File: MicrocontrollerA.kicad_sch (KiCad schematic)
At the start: 40 parts, among them J1 SWD Connector, J13 USB_B_Micro, SW1 SW_Push, SW2 SW_SPDT, SW3 SW_SPDT, U1 STM32F446RCTx, U5 TVS0500DRV, U6 TLV1117-33, Y1 25 MHz

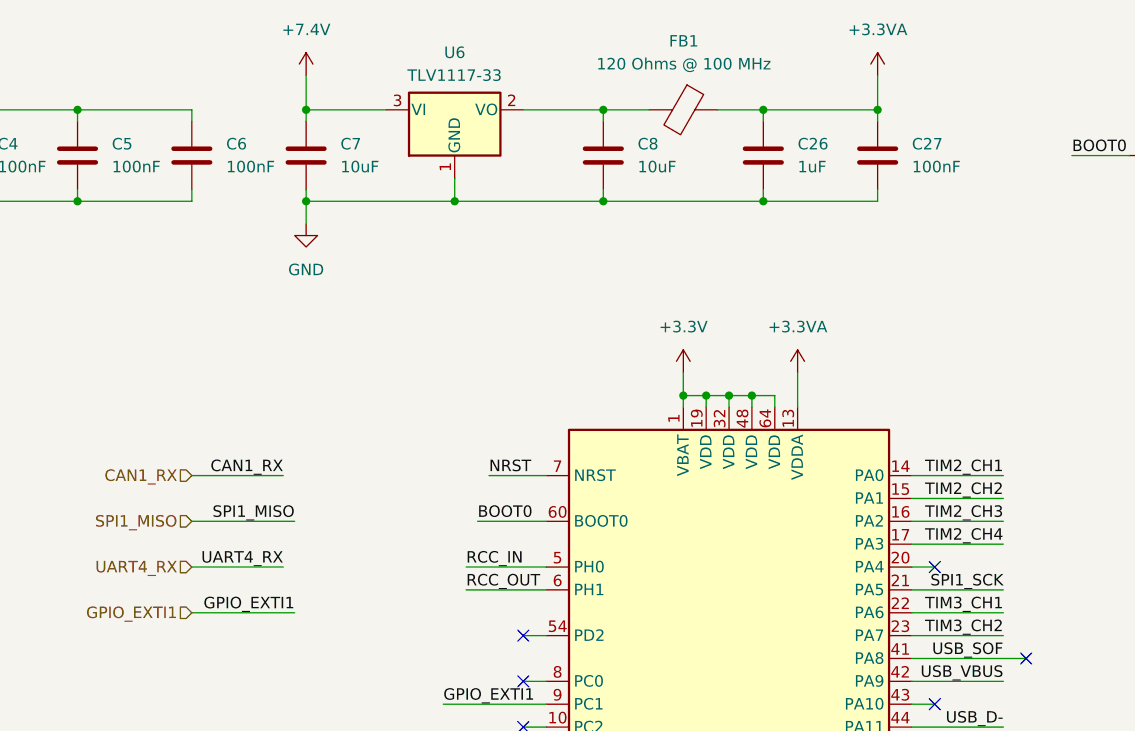
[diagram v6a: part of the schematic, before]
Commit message: Remove LDO and connect FB to switching output
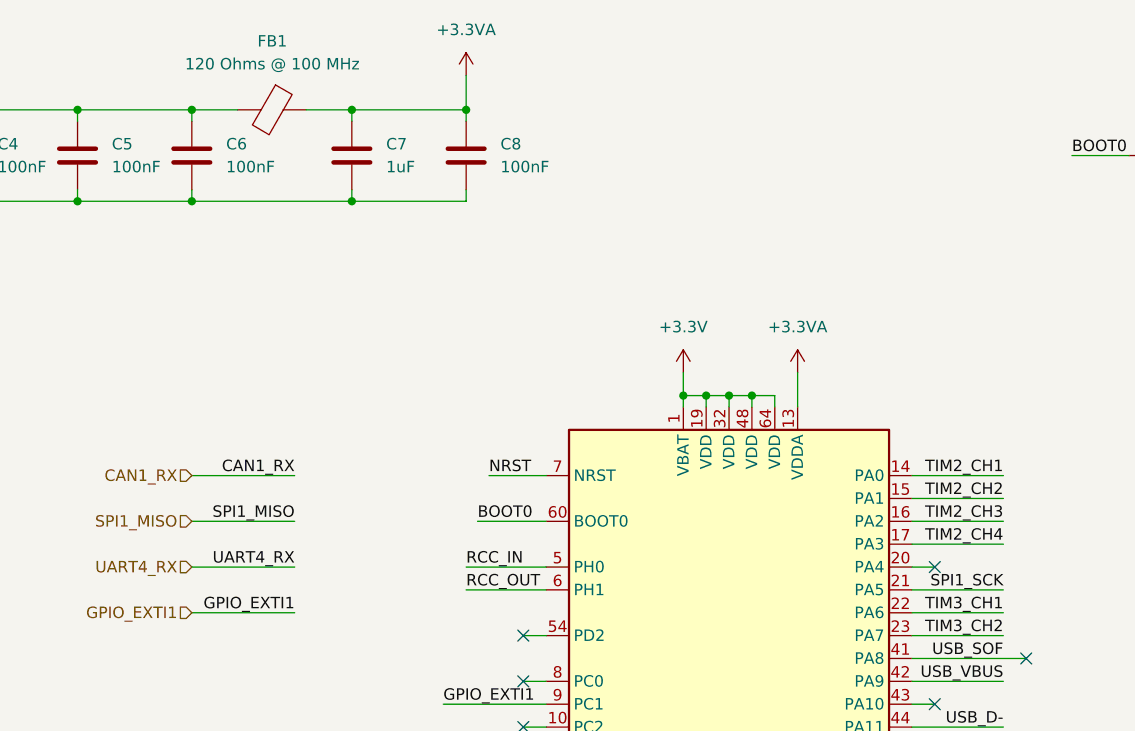
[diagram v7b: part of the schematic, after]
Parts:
- removed C7, C8: 10uF, Capacitor_SMD:C_1206_3216Metric, symbol Device:C
- removed U6: TLV1117-33, Package_TO_SOT_SMD:SOT-223-3_TabPin2, symbol Regulator_Linear:TLV1117-33
- renumbered C26 to C7, C27 to C8
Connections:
- net +3.3V: now also FB1.2
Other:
- moved on the sheet: C7, C8, FB1

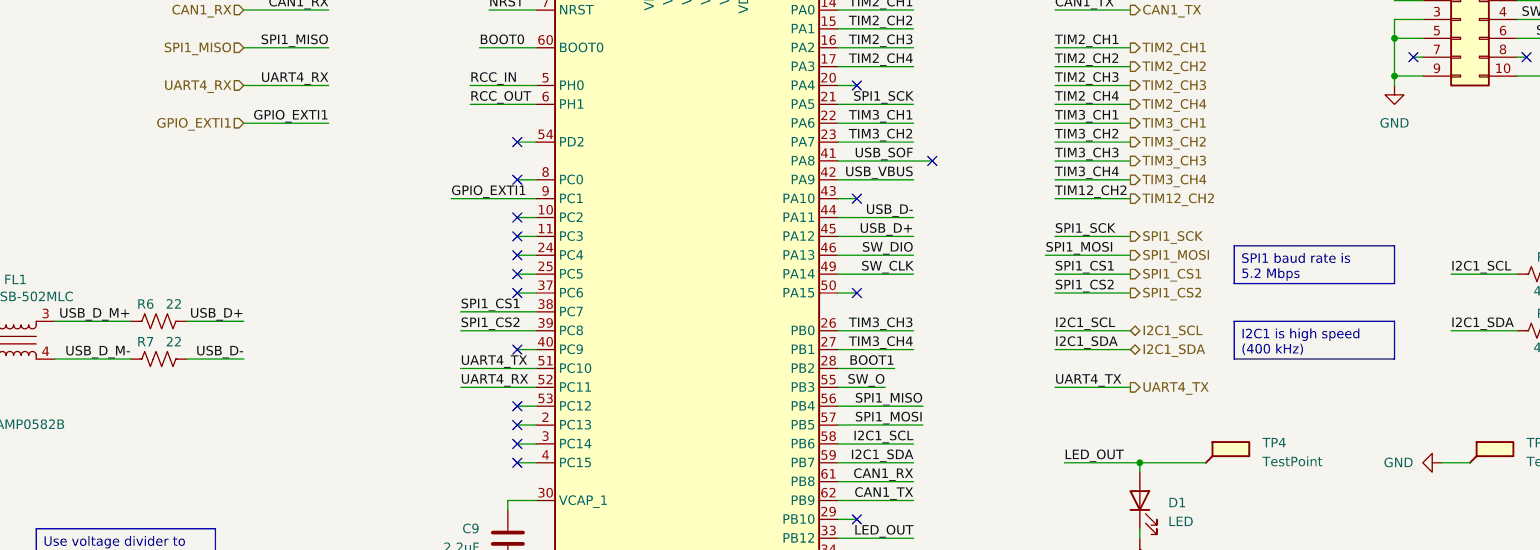
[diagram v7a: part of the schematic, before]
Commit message: Change IMU to BMI088
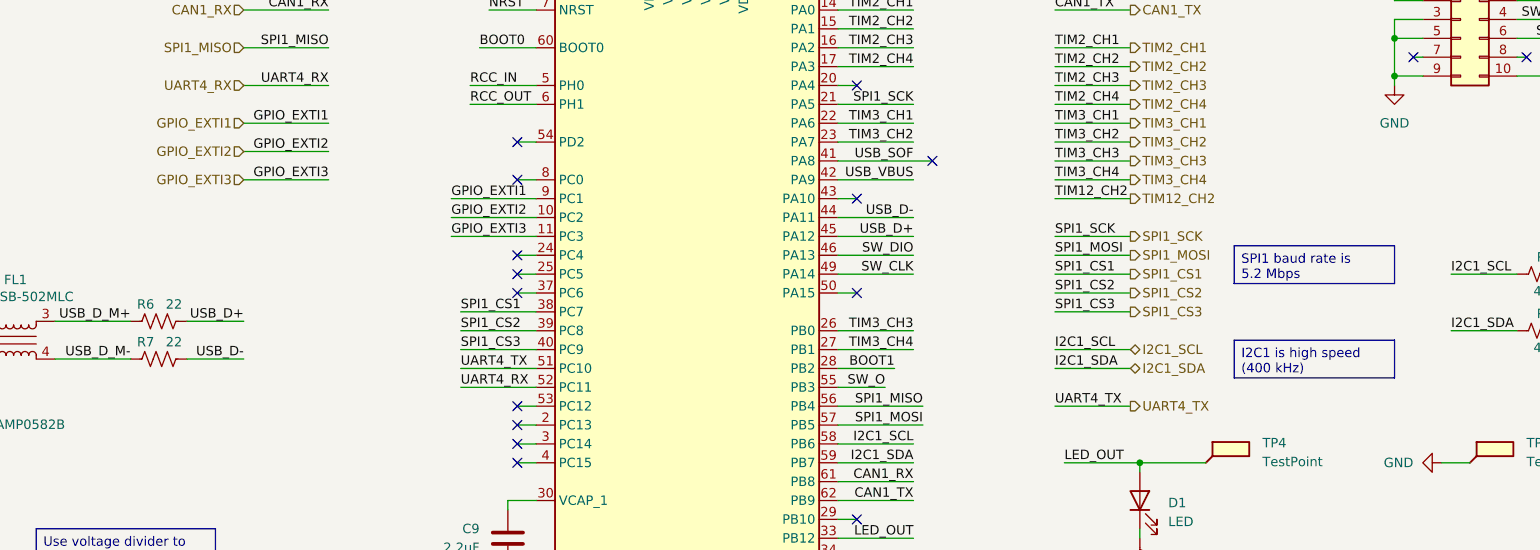
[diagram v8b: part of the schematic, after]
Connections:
- net GPIO_EXTI2: now reaches U1.10 (PC2)
- net GPIO_EXTI3: now reaches U1.11 (PC3)
- net SPI1_CS3: now reaches U1.40 (PC9)
- no-connect marks 22 -> 19
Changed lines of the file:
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@@
 	(title_block
 		(title "MCU A - STM32F446RCT6")
-		(date "2025-12-04")
+		(date "2025-12-21")
 		(rev "A")
 		(company "CU Boulder Senior Design Team 29 - Xu Lab")
@@
 	(text_box "I2C1 is high speed (400 kHz)"
 		(exclude_from_sim no)
-		(at 222.25 107.95 0)
+		(at 222.25 110.49 0)
 		(size 21.59 5.08)
 		(margins 0.9525 0.9525 0.9525 0.9525)
@@
 	)
 	(no_connect
-		(at 125.73 93.98)
-	)
-	(no_connect
 		(at 125.73 127)
 	)
@@
 	)
 	(no_connect
-		(at 125.73 96.52)
-	)
-	(no_connect
 		(at 171.45 76.2)
 	)
@@
 	)
 	(no_connect
-		(at 125.73 111.76)
-	)
-	(no_connect
 		(at 125.73 101.6)
 	)
@@
 	(wire
 		(pts
-			(xy 125.73 111.76) (xy 128.27 111.76)
-		)
-		(stroke
-			(width 0)
-			(type default)
-		)
-	)
-	(wire
-		(pts
 			(xy 41.91 107.95) (xy 49.53 107.95)
 		)
@@
 	(wire
 		(pts
+			(xy 88.9 85.09) (xy 100.33 85.09)
+		)
+		(stroke
+			(width 0)
+			(type default)
+		)
+	)
+	(wire
+		(pts
 			(xy 243.84 63.5) (xy 243.84 64.77)
 		)
@@
 	(wire
 		(pts
-			(xy 125.73 93.98) (xy 128.27 93.98)
+			(xy 119.38 21.59) (xy 119.38 25.4)
 		)
 		(stroke
@@
 	(wire
 		(pts
-			(xy 119.38 21.59) (xy 119.38 25.4)
+			(xy 198.12 88.9) (xy 208.28 88.9)
 		)
 		(stroke
@@
 	(wire
 		(pts
-			(xy 198.12 88.9) (xy 208.28 88.9)
+			(xy 44.45 113.03) (xy 44.45 115.57)
 		)
 		(stroke
@@
 	(wire
 		(pts
-			(xy 44.45 113.03) (xy 44.45 115.57)
+			(xy 153.67 57.15) (xy 153.67 58.42)
 		)
 		(stroke
@@
 	(wire
 		(pts
-			(xy 153.67 57.15) (xy 153.67 58.42)
+			(xy 76.2 35.56) (xy 88.9 35.56)
 		)
 		(stroke
@@
 	(wire
 		(pts
-			(xy 76.2 35.56) (xy 88.9 35.56)
+			(xy 125.73 101.6) (xy 128.27 101.6)
 		)
 		(stroke
@@
 	(wire
 		(pts
-			(xy 125.73 101.6) (xy 128.27 101.6)
+			(xy 260.35 69.85) (xy 267.97 69.85)
 		)
 		(stroke
@@
 	(wire
 		(pts
-			(xy 260.35 69.85) (xy 267.97 69.85)
+			(xy 116.84 93.98) (xy 128.27 93.98)
 		)
 		(stroke
@@
 	(wire
 		(pts
+			(xy 88.9 88.9) (xy 100.33 88.9)
+		)
+		(stroke
+			(width 0)
+			(type default)
+		)
+	)
+	(wire
+		(pts
 			(xy 168.91 127) (xy 179.07 127)
 		)
@@
 	(wire
 		(pts
+			(xy 116.84 96.52) (xy 128.27 96.52)
+		)
+		(stroke
+			(width 0)
+			(type default)
+		)
+	)
+	(wire
+		(pts
 			(xy 125.73 83.82) (xy 128.27 83.82)
 		)
@@
 	(wire
 		(pts
-			(xy 125.73 96.52) (xy 128.27 96.52)
-		)
-		(stroke
-			(width 0)
-			(type default)
-		)
-	)
-	(wire
-		(pts
 			(xy 25.4 35.56) (xy 38.1 35.56)
 		)
@@
 	(wire
 		(pts
-			(xy 198.12 111.76) (xy 208.28 111.76)
+			(xy 198.12 114.3) (xy 208.28 114.3)
 		)
 		(stroke
@@
 	(wire
 		(pts
-			(xy 198.12 116.84) (xy 208.28 116.84)
+			(xy 198.12 119.38) (xy 208.28 119.38)
 		)
 		(stroke
@@
 	(wire
 		(pts
+			(xy 198.12 106.68) (xy 208.28 106.68)
+		)
+		(stroke
+			(width 0)
+			(type default)
+		)
+	)
+	(wire
+		(pts
 			(xy 266.7 33.02) (xy 264.16 33.02)
 		)
@@
 	(wire
 		(pts
+			(xy 118.11 111.76) (xy 128.27 111.76)
+		)
+		(stroke
+			(width 0)
+			(type default)
+		)
+	)
+	(wire
+		(pts
 			(xy 151.13 57.15) (xy 151.13 58.42)
 		)
@@
 	(wire
 		(pts
-			(xy 198.12 109.22) (xy 208.28 109.22)
+			(xy 198.12 111.76) (xy 208.28 111.76)
 		)
 		(stroke
@@
 	(wire
 		(pts
-			(xy 196.85 99.06) (xy 208.28 99.06)
+			(xy 198.12 99.06) (xy 208.28 99.06)
 		)
 		(stroke
@@
 	)
 	(label "I2C1_SDA"
-		(at 198.12 111.76 0)
+		(at 198.12 114.3 0)
 		(effects
 			(font
@@
 		)
 	)
+	(label "GPIO_EXTI3"
+		(at 116.84 96.52 0)
+		(effects
+			(font
+				(size 1.27 1.27)
+			)
+			(justify left bottom)
+		)
+	)
+	(label "GPIO_EXTI3"
+		(at 100.33 88.9 180)
+		(effects
+			(font
+				(size 1.27 1.27)
+			)
+			(justify right bottom)
+		)
+	)
 	(label "USB_D_M-"
 		(at 73.66 113.03 180)
@@
 		)
 	)
+	(label "SPI1_CS3"
+		(at 118.11 111.76 0)
+		(effects
+			(font
+				(size 1.27 1.27)
+			)
+			(justify left bottom)
+		)
+	)
 	(label "I2C1_SCL"
 		(at 179.07 124.46 180)
@@
 		)
 	)
+	(label "GPIO_EXTI2"
+		(at 116.84 93.98 0)
+		(effects
+			(font
+				(size 1.27 1.27)
+			)
+			(justify left bottom)
+		)
+	)
 	(label "USB_D_I+"
 		(at 53.34 107.95 180)
@@
 		)
 	)
+	(label "SPI1_CS3"
+		(at 198.12 106.68 0)
+		(effects
+			(font
+				(size 1.27 1.27)
+			)
+			(justify left bottom)
+		)
+	)
 	(label "SW_CLK"
 		(at 267.97 67.31 180)
@@
 		)
 	)
+	(label "GPIO_EXTI2"
+		(at 100.33 85.09 180)
+		(effects
+			(font
+				(size 1.27 1.27)
+			)
+			(justify right bottom)
+		)
+	)
 	(label "BOOT1"
 		(at 176.53 114.3 180)
@@
 	)
 	(label "UART4_TX"
-		(at 198.12 116.84 0)
+		(at 198.12 119.38 0)
 		(effects
 			(font
@@
 	)
 	(label "I2C1_SCL"
-		(at 198.12 109.22 0)
+		(at 198.12 111.76 0)
 		(effects
 			(font
@@
 	)
 	(label "SPI1_MOSI"
-		(at 196.85 99.06 0)
+		(at 198.12 99.06 0)
 		(effects
 			(font
@@
 	(hierarchical_label "I2C1_SDA"
 		(shape bidirectional)
-		(at 208.28 111.76 0)
+		(at 208.28 114.3 0)
 		(effects
 			(font
@@
 		)
 	)
+	(hierarchical_label "GPIO_EXTI2"
+		(shape input)
+		(at 88.9 85.09 180)
+		(effects
+			(font
+				(size 1.27 1.27)
+			)
+			(justify right)
+		)
+	)
 	(hierarchical_label "SPI1_SCK"
 		(shape output)
@@
 		)
 	)
+	(hierarchical_label "GPIO_EXTI3"
+		(shape input)
+		(at 88.9 88.9 180)
+		(effects
+			(font
+				(size 1.27 1.27)
+			)
+			(justify right)
+		)
+	)
 	(hierarchical_label "TIM3_CH3"
 		(shape output)
@@
 	(hierarchical_label "UART4_TX"
 		(shape output)
-		(at 208.28 116.84 0)
+		(at 208.28 119.38 0)
 		(effects
 			(font
@@
 	(hierarchical_label "I2C1_SCL"
 		(shape bidirectional)
-		(at 208.28 109.22 0)
+		(at 208.28 111.76 0)
 		(effects
 			(font
@@
 		(effects
 			(font
+				(size 1.27 1.27)
+			)
+			(justify left)
+		)
+	)
+	(hierarchical_label "SPI1_CS3"
+		(shape output)
+		(at 208.28 106.68 0)
+		(effects
+			(font
